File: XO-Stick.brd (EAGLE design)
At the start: 74.9 x 53.3 mm, 30 parts, among them J1 POWER, J2 85MOTR, J3 85MOTL, J4 REF, J5 SCL, J6 SDA, J7 AVCC (N/C), J8 AGND (N/C), J9 EXT VCC, SW1 USER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

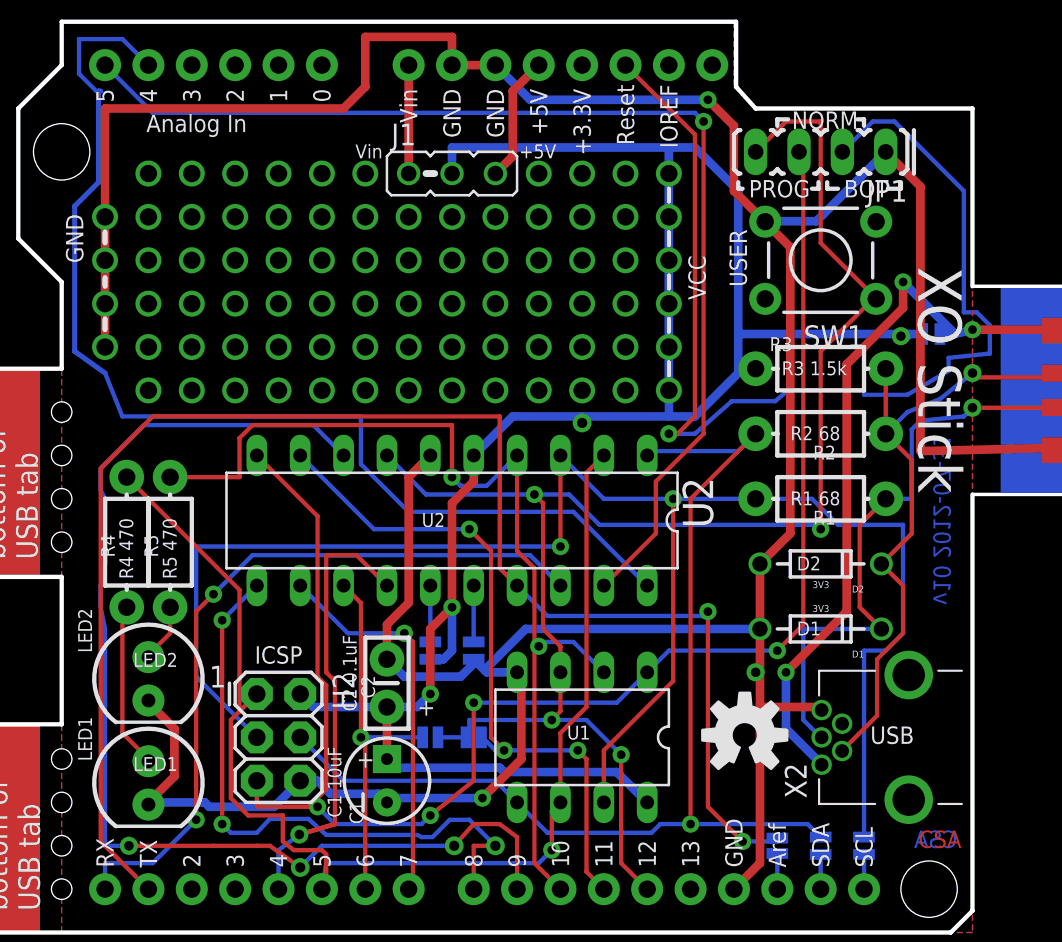
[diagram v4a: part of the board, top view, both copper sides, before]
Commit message: Tweak USB mini-B connector footprint; restring to 8mil min.
USB connector footprint was restricting the min pad width in our restring.
Noticed that USB footprint was really loose, too.  Checked against datasheet,
tightened up holes and switched to oblong pads.  Restring to 8mil min,
which required a few minor trace adjustments.
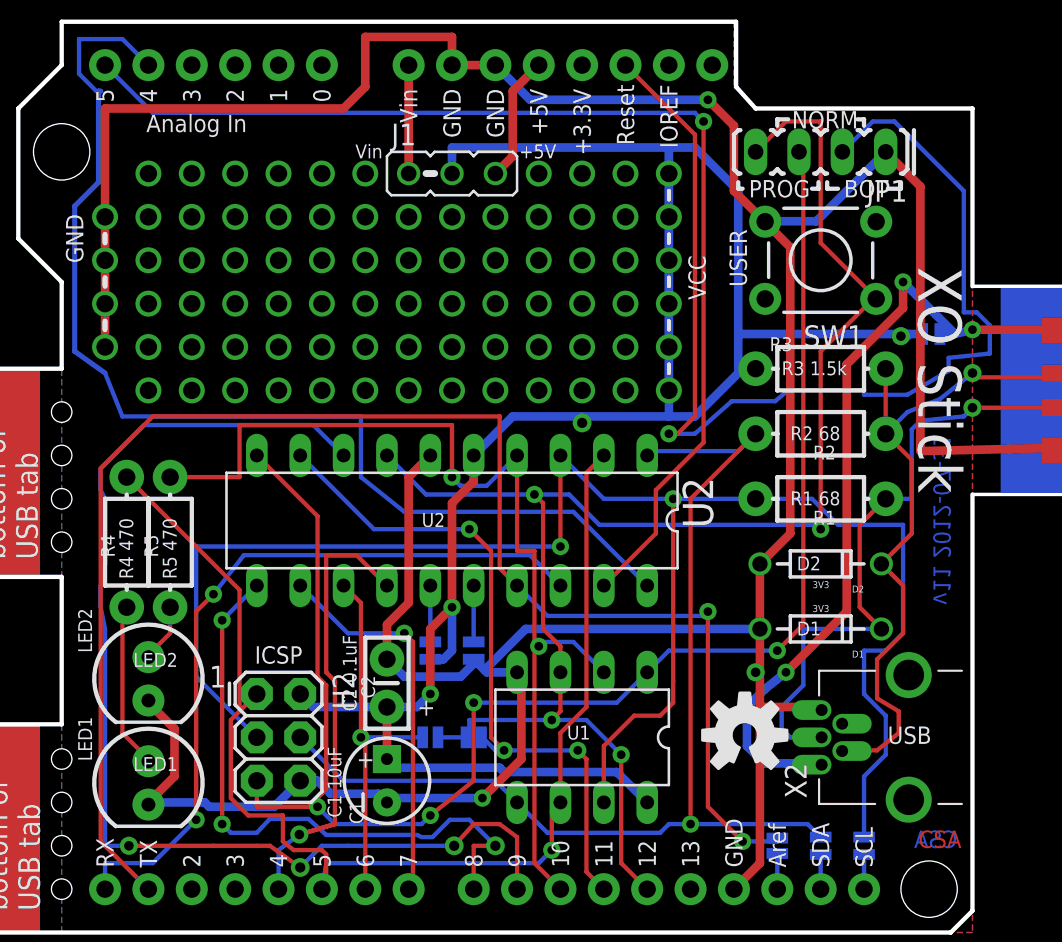
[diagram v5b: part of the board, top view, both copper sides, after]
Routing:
- net VBUS: track 46.0 -> 50.0 mm
- net USB-D_M: track 39.8 -> 42.3 mm
- net USB-D_P: track 37.1 -> 39.2 mm
- net D_P: track 100.5 -> 102.5 mm
- net D3: track 58.3 -> 59.3 mm
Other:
- board text added: "PB0"
- board text added: "PB2"
- board text added: "SCL/"
- board text added: "SDA/"
- board text added: "v11 2012-07-31"
- board text removed: "SCL/PB2"
- board text removed: "SDA/PB0"
- board text removed: "v10 2012-07-31"

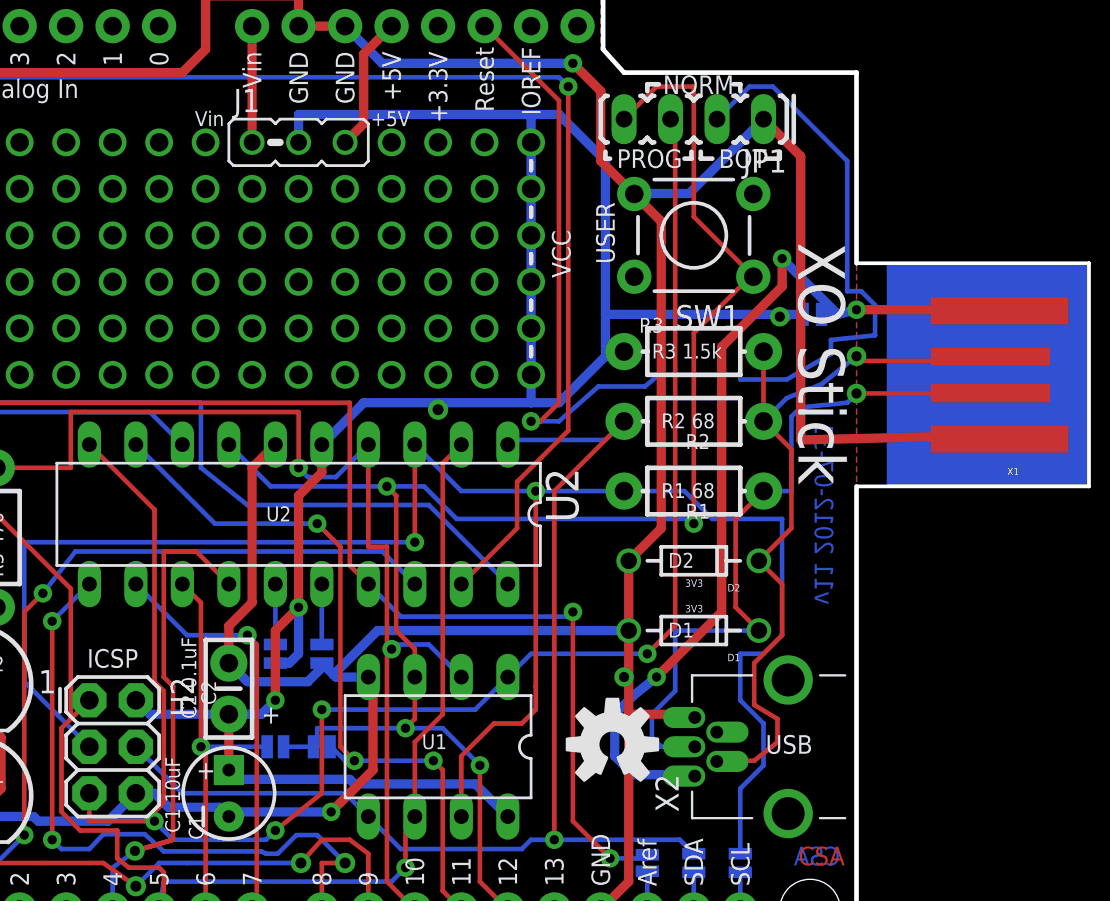
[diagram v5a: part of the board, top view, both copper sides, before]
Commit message: Add optional 3.3v TO-92 LDO regulator, for use when unbricking XOs.
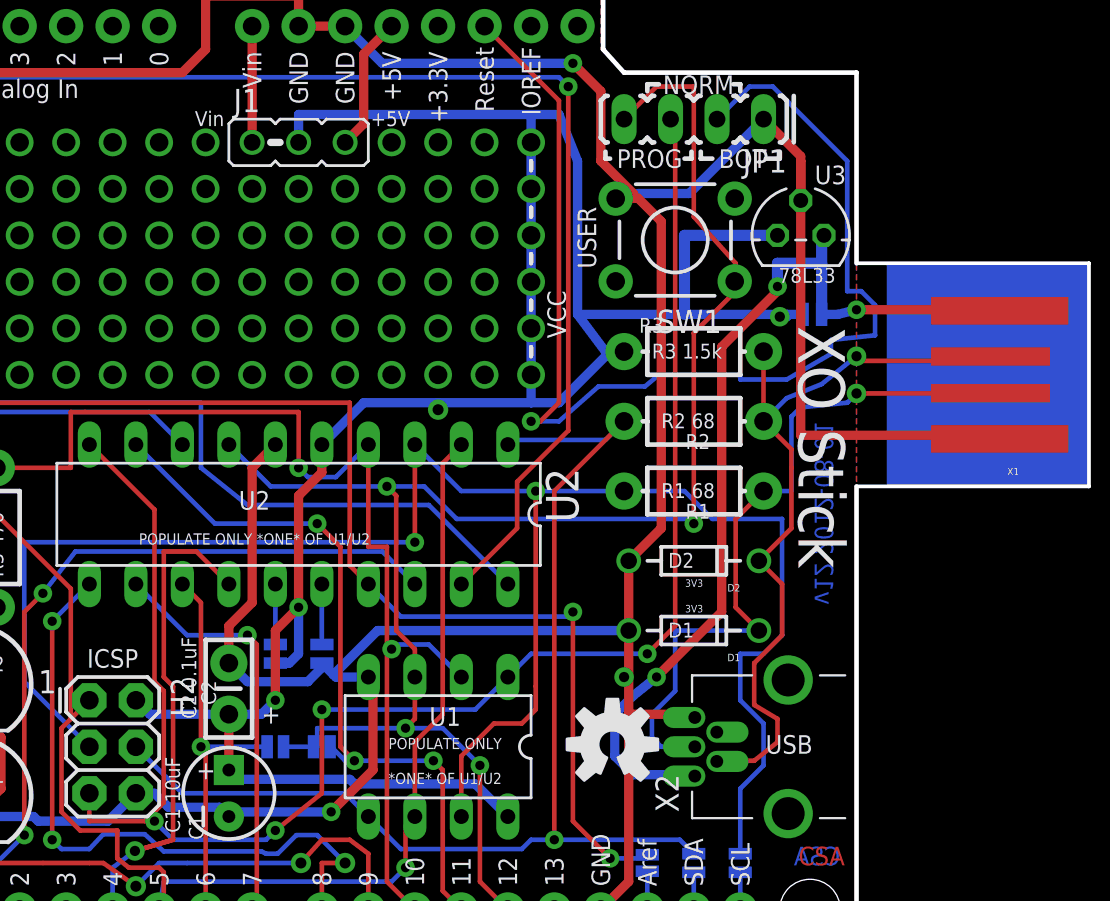
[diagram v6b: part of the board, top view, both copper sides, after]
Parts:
- added H1: ARDUINO-SHIELD, xorduino:ARDUINO-SHIELD-VIAS-HOLES
- U3: value ARDUINO-SHIELD -> L78L33ACZ; device xorduino:ARDUINO-SHIELD-VIAS-HOLES -> linear:TO92
- moved U3 63.9 mm to (59.2, 39.4)
- moved SW1 1.05 mm to (52.3, 39.1)
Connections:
- net ARD_5V: now also H1.5V; no longer U3.5V
- net ARD_RST: now also H1.RES; no longer U3.RES
- net ARD_VIN: now also H1.VIN; no longer U3.VIN
- net AREF: now also H1.AREF; no longer U3.AREF
- net D1: now also H1.D5; no longer U3.D5
- net D3: now also H1.D10; no longer U3.D10
- net D4: now also H1.D12; no longer U3.D12
- net GND: now also H1.GND@0, H1.GND@1, H1.GND@2, U3.2; no longer U3.GND@0, U3.GND@1, U3.GND@2
- net PA0: now also H1.A4; no longer U3.A4
- net PA1: now also H1.A5; no longer U3.A5
- net PA2: now also H1.RX; no longer U3.RX
- net PA3: now also H1.TX; no longer U3.TX
- net PA4: now also H1.D4; no longer U3.D4
- net PA5: now also H1.D6; no longer U3.D6
- net PA6: now also H1.D7; no longer U3.D7
- net PA7: now also H1.D8; no longer U3.D8
- net PB5: now also H1.D9; no longer U3.D9
- net PB6: now also H1.D11; no longer U3.D11
- net SCL: now also H1.SCL; no longer U3.SCL
- net SDA: now also H1.SDA; no longer U3.SDA
- net VBUS: now also U3.3
- net VCC: now also U3.1
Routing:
- net VCC: track 123.2 -> 133.8 mm
- net GND: track 222.9 -> 227.7 mm
- net VBUS: track 50.0 -> 52.5 mm
- net D4: track 93.5 -> 92.5 mm
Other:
- board text added: "*ONE* OF U1/U2"
- board text added: "78L33"
- board text added: "CUT VBUS IF U3 INSTALLED"
- board text added: "POPULATE ONLY"
- board text added: "POPULATE ONLY *ONE* OF U1/U2"
- board text added: "U3"
- board text added: "v12 2012-08-01"
- board text removed: "v11 2012-07-31"

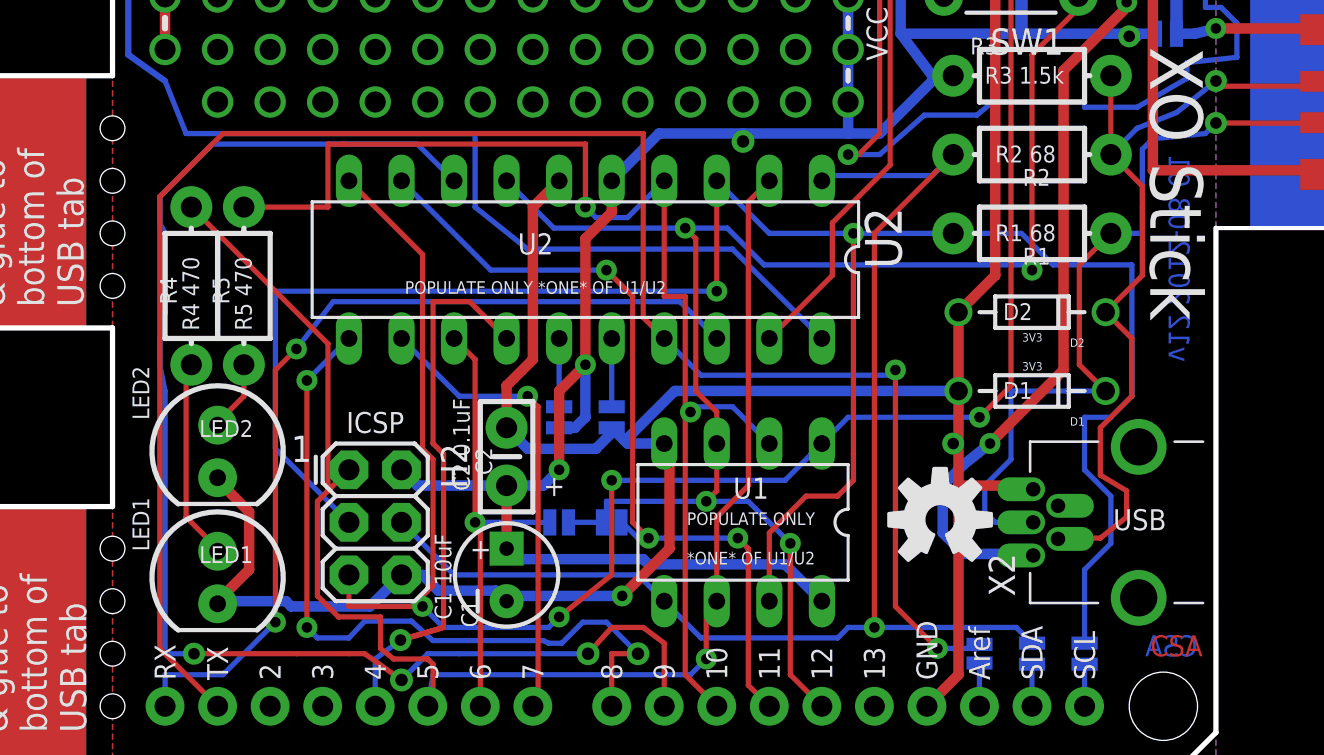
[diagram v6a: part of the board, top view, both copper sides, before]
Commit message: XO Stick v13: silkscreen additions; rename nets in schematic for less confusion.
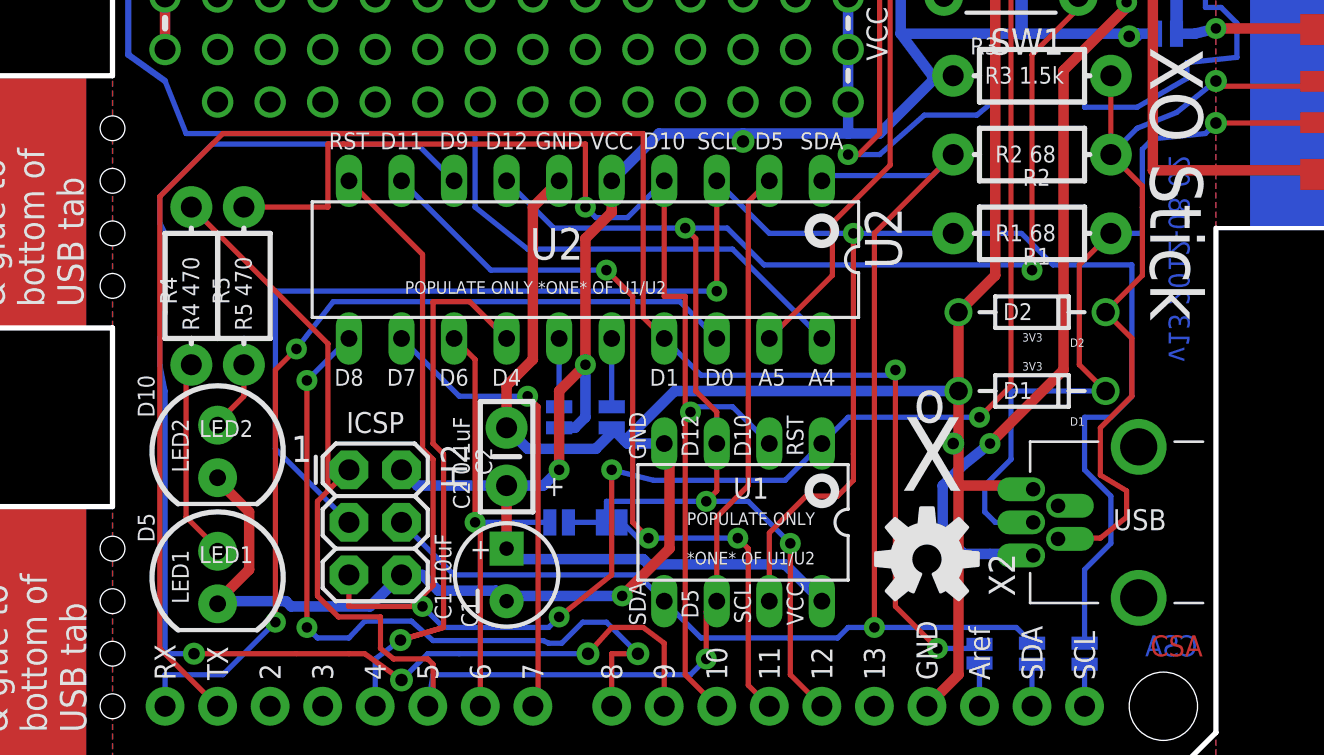
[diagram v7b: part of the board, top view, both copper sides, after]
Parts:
- moved U$1 2.01 mm to (48.3, 9.65)
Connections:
- net D1 renamed PB1
- net D3 renamed PB3
- net D4 renamed PB4
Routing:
- net RST: track 91.7 -> 92.2 mm
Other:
- board text added: "A4"
- board text added: "A5"
- board text added: "AGND"
- board text added: "AVCC"
- board text added: "D0"
- board text added: "D10"
- board text added: "D11"
- board text added: "D12"
- board text added: "D4"
- board text added: "D5"
- board text added: "D6"
- board text added: "D7"
- board text added: "D8"
- board text added: "D9"
- board text added: "RESET"
- board text added: "SCL"
- board text added: "SDA"
- board text added: "X"
- board text added: "o"
- board text added: "v13 2012-08-02"
- board text removed: "Reset"
- board text removed: "v12 2012-08-01"
